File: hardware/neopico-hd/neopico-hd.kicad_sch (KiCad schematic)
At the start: 19 parts, among them J1 HDMI_A, U1 SN74LVC2G14DBV, U2 SN74LVC2G14DBV, U3 SN74LVC245APW, U4 SN74LVC245APW, U5 SN74LVC245APW, U6 ESD224DQA, U7 ESD224DQA

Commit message: Starting PCB
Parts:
- removed U6, U7: ESD224DQA, Package_DFN_QFN:Diodes_UDFN-10_1.0x2.5mm_P0.5mm, symbol Power_Protection:ESD224DQA
- added J2, J3, J4: Conn_01x05_Socket, Connector_JST:JST_XH_B5B-XH-A_1x05_P2.50mm_Vertical, symbol Connector:Conn_01x05_Socket
- added J5, J6: Conn_01x05_Socket, symbol Connector:Conn_01x05_Socket
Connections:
- net HDMI_CLK+ is gone; now on net CLK+: J1.10 (CK+)
- net HDMI_CLK- is gone; now on net CLK-: J1.12 (CK-)
- net HDMI_D0+ is gone; now on net D0+: J1.7 (D0+)
- net HDMI_D0- is gone; now on net D0-: J1.9 (D0-)
- net HDMI_D1+ is gone; now on net D1+: J1.4 (D1+)
- net HDMI_D1- is gone; now on net D1-: J1.6 (D1-)
- net HDMI_D2+ is gone; now on net D2+: J1.1 (D2+)
- net HDMI_D2- is gone; now on net D2-: J1.3 (D2-)
- net CLK+: now also A1.19 (GPIO13); no longer A1.24 (GPIO18)
- net CLK-: now also A1.18 (GPIO12); no longer A1.25 (GPIO19)
- net D0+: now also A1.21 (GPIO15); no longer A1.22 (GPIO16)
- net D0-: now also A1.20 (GPIO14); no longer A1.23 (GPIO17)
- net D1+: now also A1.23 (GPIO17); no longer A1.20 (GPIO14)
- net D1-: now also A1.22 (GPIO16); no longer A1.21 (GPIO15)
- net D2+: now also A1.25 (GPIO19); no longer A1.18 (GPIO12)
- net D2-: now also A1.24 (GPIO18); no longer A1.19 (GPIO13)
- net DARK: now also U5.18 (B1)
- net DAT: now also U5.16 (B3); no longer U5.18 (B1)
- net MVS_B0: now also J4.1 (Pin_1)
- net MVS_B1: now also J4.2 (Pin_2)
- net MVS_B2: now also J4.3 (Pin_3)
- net MVS_B3: now also J4.4 (Pin_4)
- net MVS_B4: now also J4.5 (Pin_5)
- net MVS_BCK: now also J6.3 (Pin_3)
- net MVS_CSYNC: now also J5.2 (Pin_2)
- net MVS_DAT: now also U5.4 (A3), J6.1 (Pin_1); no longer U5.2 (A1)
- net MVS_G0: now also J3.1 (Pin_1)
- net MVS_G1: now also J3.2 (Pin_2)
- net MVS_G2: now also J3.3 (Pin_3)
- net MVS_G3: now also J3.4 (Pin_4)
- net MVS_G4: now also J3.5 (Pin_5)
- net MVS_PCKL: now also J5.1 (Pin_1)
- net MVS_R0: now also J2.1 (Pin_1)
- net MVS_R1: now also J2.2 (Pin_2)
- net MVS_R2: now also J2.3 (Pin_3)
- net MVS_R3: now also J2.4 (Pin_4)
- net MVS_R4: now also J2.5 (Pin_5)
- net MVS_WS: now also U5.5 (A4), J6.2 (Pin_2); no longer U5.3 (A2)
- net WS: now also U5.15 (B4); no longer U5.17 (B2)
- net SHADOW renamed SHD
- net SHD: now also U5.17 (B2)
- new net MVS_DARK: J5.3 (Pin_3), U5.2 (A1)
- new net MVS_SHD: J5.4 (Pin_4), U5.3 (A2)
- no-connect marks 31 -> 29
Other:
- moved on the sheet: A1, C1, C2, C3, C4, C5, C6, C7, D1, F1, FB1, J1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

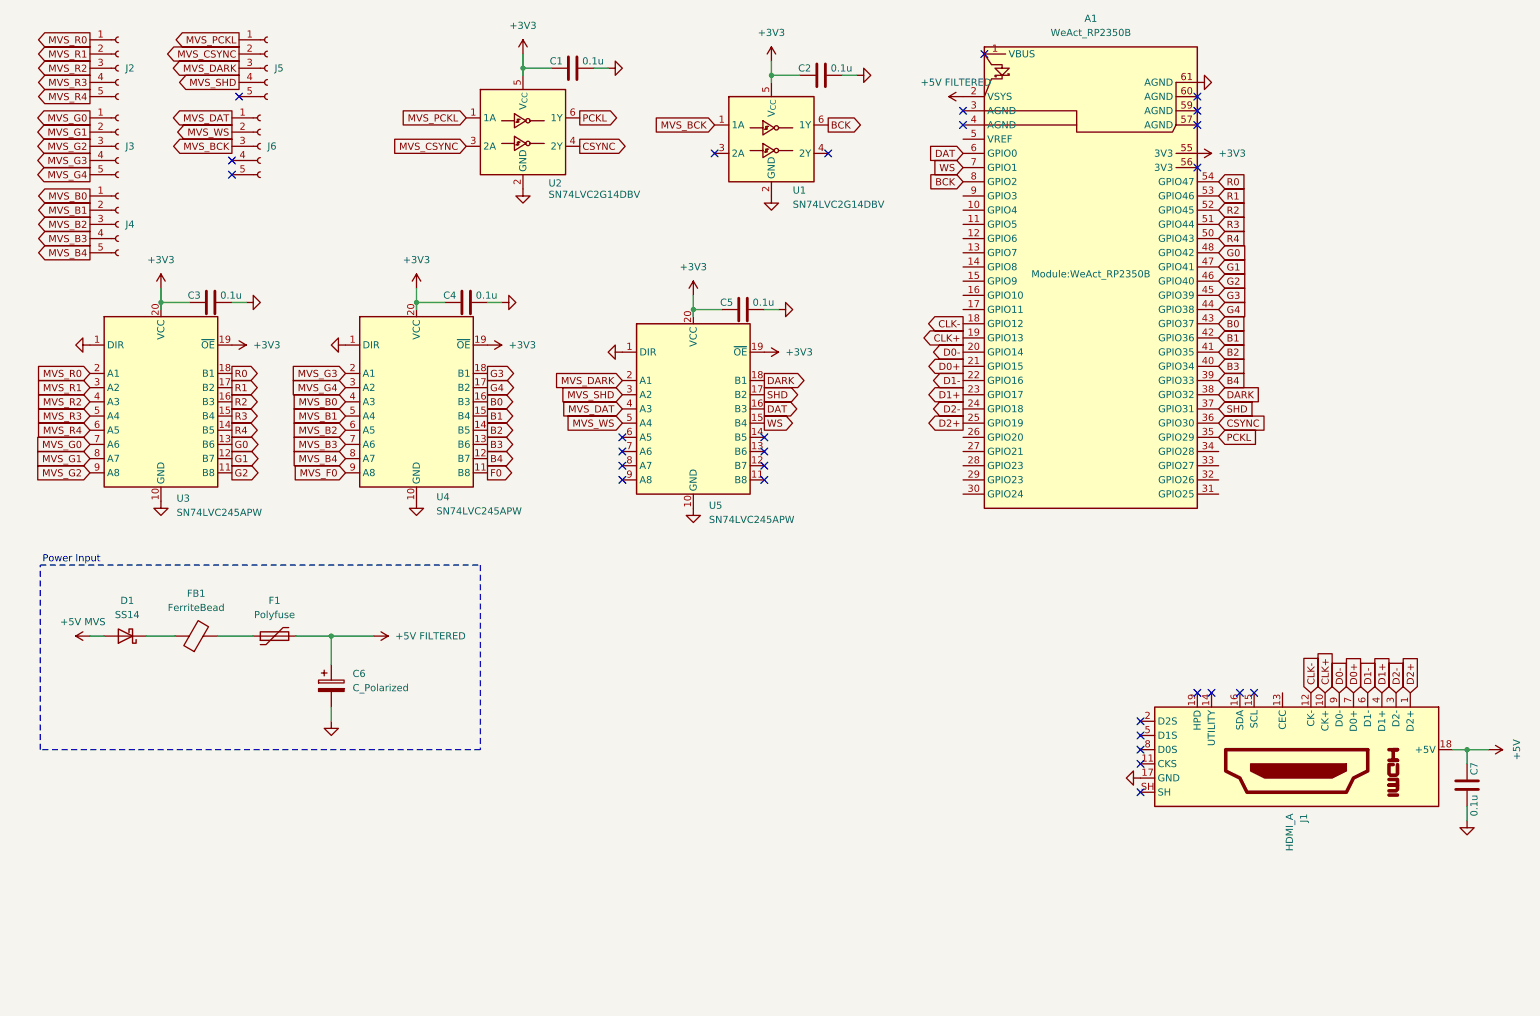
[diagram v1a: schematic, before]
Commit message: GP25+ video capture working
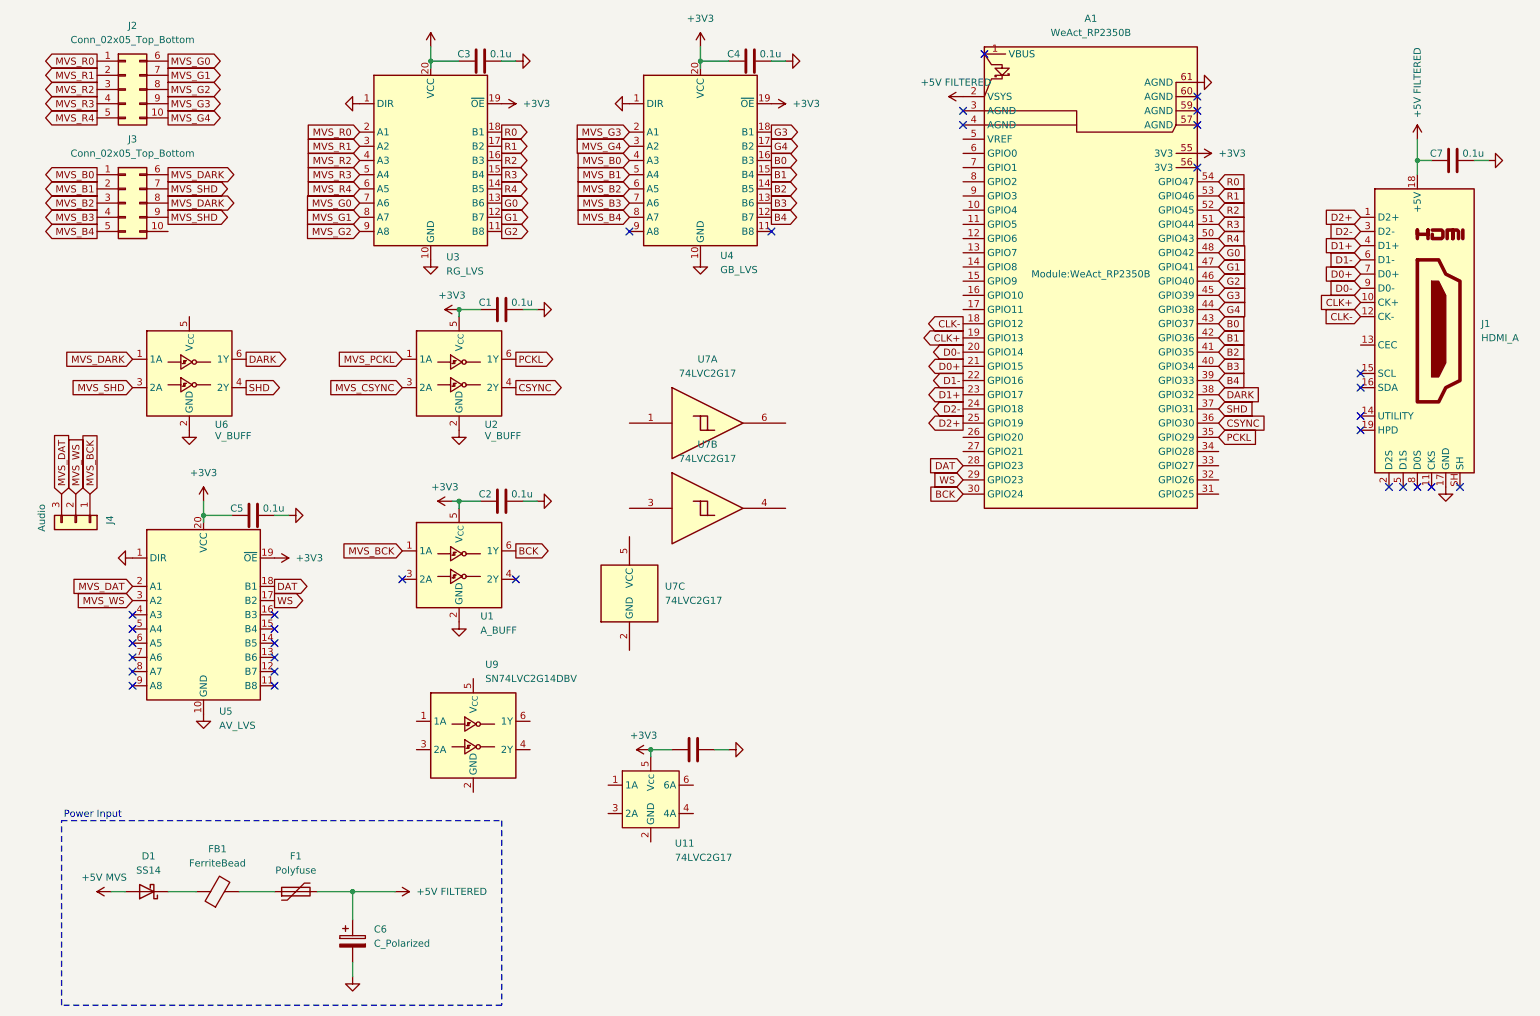
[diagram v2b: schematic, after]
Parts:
- removed J2, J3, J4: Conn_01x05_Socket, Connector_JST:JST_XH_B5B-XH-A_1x05_P2.50mm_Vertical, symbol Connector:Conn_01x05_Socket
- removed J5, J6: Conn_01x05_Socket, symbol Connector:Conn_01x05_Socket
- added C8: 0.1u, Capacitor_SMD:C_0805_2012Metric_Pad1.18x1.45mm_HandSolder, symbol Device:C
- added J2, J3: Conn_02x05_Top_Bottom, Connector_IDC:IDC-Header_2x05_P2.54mm_Vertical, symbol Connector_Generic:Conn_02x05_Top_Bottom
- added J4: Audio, Connector_JST:JST_XA_B03B-XASK-1_1x03_P2.50mm_Vertical, symbol Connector_Generic:Conn_01x03
- added U11: 74LVC2G17, Package_TO_SOT_SMD:TSOT-23-6_HandSoldering, symbol neopico-hd:74LVC2G17
- added U6: V_BUFF, Package_TO_SOT_SMD:SOT-23-6, symbol 74xGxx:SN74LVC2G14DBV
- added U7: 74LVC2G17, symbol 74xGxx:74LVC2G17
- added U9: SN74LVC2G14DBV, Package_TO_SOT_SMD:SOT-23-6, symbol 74xGxx:SN74LVC2G14DBV
- C1, C2, C3, C4, C5, C7: footprint custom_components:SM0603_Capa_libcms -> Capacitor_SMD:C_0805_2012Metric_Pad1.18x1.45mm_HandSolder
- F1, FB1: footprint (none) -> Capacitor_SMD:C_0805_2012Metric
- U1: value SN74LVC2G14DBV -> A_BUFF
- U2: value SN74LVC2G14DBV -> V_BUFF
- U3: value SN74LVC245APW -> RG_LVS
- U4: value SN74LVC245APW -> GB_LVS
- U5: value SN74LVC245APW -> AV_LVS
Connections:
- net +5V is gone; now on net +5V FILTERED: C7.1, J1.18 (+5V)
- net +3V3: now also C8.1, U11.5 (Vcc)
- net BCK: now also A1.30 (GPIO24); no longer A1.8 (GPIO2)
- net DARK: now also U6.6 (1Y); no longer U5.18 (B1)
- net DAT: now also A1.28 (GPIO23), U5.18 (B1); no longer A1.6 (GPIO0), U5.16 (B3)
- net GND: now also C8.2, U6.2 (GND)
- net MVS_B0: now also J3.1 (Pin_1)
- net MVS_B1: now also J3.2 (Pin_2)
- net MVS_B2: now also J3.3 (Pin_3)
- net MVS_B3: now also J3.4 (Pin_4)
- net MVS_B4: now also J3.5 (Pin_5)
- net MVS_BCK: now also J4.1 (Pin_1)
- net MVS_DARK: now also J3.6 (Pin_6), J3.8 (Pin_8), U6.1 (1A); no longer U5.2 (A1)
- net MVS_DAT: now also U5.2 (A1), J4.3 (Pin_3); no longer U5.4 (A3)
- net MVS_G0: now also J2.6 (Pin_6)
- net MVS_G1: now also J2.7 (Pin_7)
- net MVS_G2: now also J2.8 (Pin_8)
- net MVS_G3: now also J2.9 (Pin_9)
- net MVS_G4: now also J2.10 (Pin_10)
- net MVS_R0: now also J2.1 (Pin_1)
- net MVS_R1: now also J2.2 (Pin_2)
- net MVS_R2: now also J2.3 (Pin_3)
- net MVS_R3: now also J2.4 (Pin_4)
- net MVS_R4: now also J2.5 (Pin_5)
- net MVS_SHD: now also J3.7 (Pin_7), J3.9 (Pin_9), U6.3 (2A); no longer U5.3 (A2)
- net MVS_WS: now also U5.3 (A2), J4.2 (Pin_2); no longer U5.5 (A4)
- net SHD: now also U6.4 (2Y); no longer U5.17 (B2)
- net WS: now also A1.29 (GPIO23), U5.17 (B2); no longer A1.7 (GPIO1), U5.15 (B4)
- net F0: no longer names the net of U4.11 (B8)
- net MVS_F0: no longer names the net of U4.9 (A8)
- no-connect marks 29 -> 32
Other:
- moved on the sheet: C1, C2, C3, C4, C5, C6, C7, D1, F1, FB1, J1, U1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
